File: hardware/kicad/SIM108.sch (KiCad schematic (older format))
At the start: 28 parts, among them J1 Screw_Terminal_01x09, J2 CAN, SW1 PRG, SW2 INSTANCE, SW3 BUS, U1 MCP2551-I-P, U2 TMR_2411, U3 MAX6816, U4 74HC595, U5 Teensy_3.2

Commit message: Stuff
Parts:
- R3: value 4K7 -> 470R
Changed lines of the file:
@@
 P 10150 4300
 F 0 "R3" H 10100 4300 50  0000 R CNN
-F 1 "4K7" V 10150 4300 39  0000 C CNN
+F 1 "470R" V 10150 4300 39  0000 C CNN
 F 2 "Resistor_THT:R_Axial_DIN0207_L6.3mm_D2.5mm_P2.54mm_Vertical" V 10080 4300 50  0001 C CNN
 F 3 "~" H 10150 4300 50  0001 C CNN

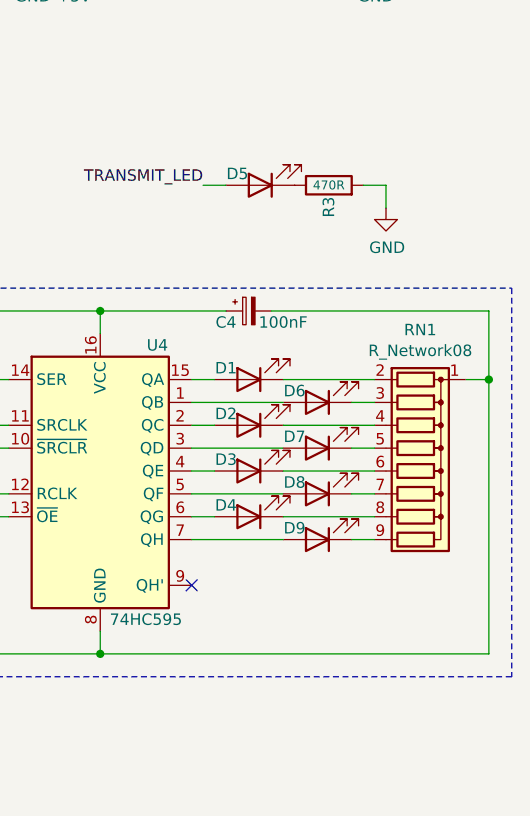
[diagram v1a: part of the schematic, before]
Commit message: Add mount holes
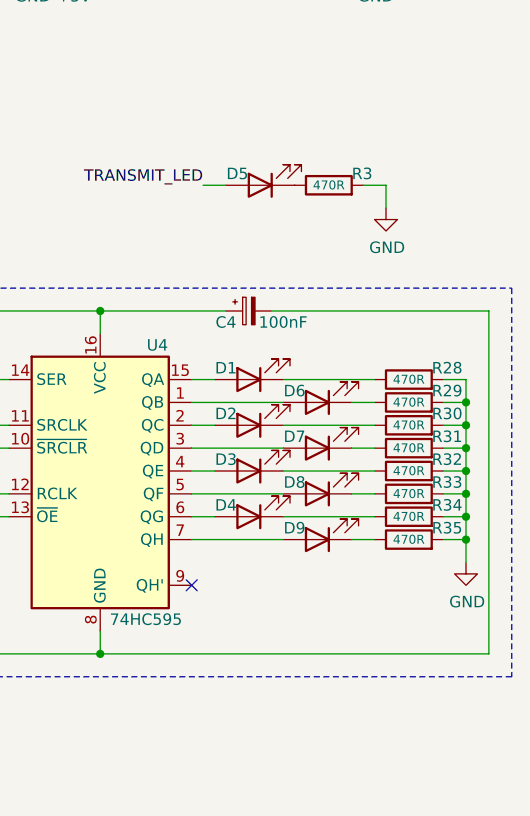
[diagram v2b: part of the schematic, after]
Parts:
- removed RN1: R_Network08, Resistor_THT:R_Array_SIP9, symbol Device:R_Network08
- added R28, R29, R30, R31, R32, R33, R34, R35: 470R, Resistor_THT:R_Axial_DIN0207_L6.3mm_D2.5mm_P2.54mm_Vertical, symbol Device:R
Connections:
- net GND: now also R28.2, R29.2, R30.2, R31.2, R32.2, R33.2, R34.2, R35.2
- net at D1.1 (K): now also R28.1
- net at D6.1 (K): now also R29.1
- net at D2.1 (K): now also R30.1
- net at D7.1 (K): now also R31.1
- net at D4.1 (K): now also R34.1
- net at D9.1 (K): now also R35.1
- net at D3.1 (K): now also R32.1
- net at D8.1 (K): now also R33.1
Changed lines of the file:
@@
 $EndComp
-Wire Wire Line
-	10750 5150 10850 5150
 Wire Wire Line
 	10850 6350 9150 6350
@@
 Wire Wire Line
 	9950 5750 10350 5750
-$Comp
-L Device:R_Network08 RN1
-U 1 1 6337568A
-P 10550 5550
-F 0 "RN1" V 9933 5550 50  0000 C CNN
-F 1 "R_Network08" V 10024 5550 50  0000 C CNN
-F 2 "Resistor_THT:R_Array_SIP9" V 11025 5550 50  0001 C CNN
-F 3 "http://www.vishay.com/docs/31509/csc.pdf" H 10550 5550 50  0001 C CNN
-	1    10550 5550
-	0    1    1    0
-$EndComp
-Wire Wire Line
-	10850 5150 10850 6350
 Wire Wire Line
 	10250 5850 10350 5850
@@
 Wire Wire Line
 	9900 4850 10850 4850
-Wire Wire Line
-	10850 4850 10850 5150
-Connection ~ 10850 5150
 $Comp
 L Switch:SW_Push SW1
@@
 U 1 1 63493E4A
 P 10150 4300
-F 0 "R3" H 10100 4300 50  0000 R CNN
+F 0 "R3" V 10200 4200 50  0000 R CNN
 F 1 "470R" V 10150 4300 39  0000 C CNN
 F 2 "Resistor_THT:R_Axial_DIN0207_L6.3mm_D2.5mm_P2.54mm_Vertical" V 10080 4300 50  0001 C CNN
@@
 	0    -1   1    0
 $EndComp
+$Comp
+L Device:R R28
+U 1 1 634C34EB
+P 10500 5150
+F 0 "R28" V 10550 5050 50  0000 R CNN
+F 1 "470R" V 10500 5150 39  0000 C CNN
+F 2 "Resistor_THT:R_Axial_DIN0207_L6.3mm_D2.5mm_P2.54mm_Vertical" V 10430 5150 50  0001 C CNN
+F 3 "~" H 10500 5150 50  0001 C CNN
+	1    10500 5150
+	0    -1   -1   0
+$EndComp
+$Comp
+L Device:R R29
+U 1 1 634C3A8E
+P 10500 5250
+F 0 "R29" V 10550 5150 50  0000 R CNN
+F 1 "470R" V 10500 5250 39  0000 C CNN
+F 2 "Resistor_THT:R_Axial_DIN0207_L6.3mm_D2.5mm_P2.54mm_Vertical" V 10430 5250 50  0001 C CNN
+F 3 "~" H 10500 5250 50  0001 C CNN
+	1    10500 5250
+	0    -1   -1   0
+$EndComp
+$Comp
+L Device:R R30
+U 1 1 634C3E87
+P 10500 5350
+F 0 "R30" V 10550 5250 50  0000 R CNN
+F 1 "470R" V 10500 5350 39  0000 C CNN
+F 2 "Resistor_THT:R_Axial_DIN0207_L6.3mm_D2.5mm_P2.54mm_Vertical" V 10430 5350 50  0001 C CNN
+F 3 "~" H 10500 5350 50  0001 C CNN
+	1    10500 5350
+	0    -1   -1   0
+$EndComp
+$Comp
+L Device:R R31
+U 1 1 634C42EC
+P 10500 5450
+F 0 "R31" V 10550 5350 50  0000 R CNN
+F 1 "470R" V 10500 5450 39  0000 C CNN
+F 2 "Resistor_THT:R_Axial_DIN0207_L6.3mm_D2.5mm_P2.54mm_Vertical" V 10430 5450 50  0001 C CNN
+F 3 "~" H 10500 5450 50  0001 C CNN
+	1    10500 5450
+	0    -1   -1   0
+$EndComp
+$Comp
+L Device:R R32
+U 1 1 634C469C
+P 10500 5550
+F 0 "R32" V 10550 5450 50  0000 R CNN
+F 1 "470R" V 10500 5550 39  0000 C CNN
+F 2 "Resistor_THT:R_Axial_DIN0207_L6.3mm_D2.5mm_P2.54mm_Vertical" V 10430 5550 50  0001 C CNN
+F 3 "~" H 10500 5550 50  0001 C CNN
+	1    10500 5550
+	0    -1   -1   0
+$EndComp
+$Comp
+L Device:R R33
+U 1 1 634C4AC7
+P 10500 5650
+F 0 "R33" V 10550 5550 50  0000 R CNN
+F 1 "470R" V 10500 5650 39  0000 C CNN
+F 2 "Resistor_THT:R_Axial_DIN0207_L6.3mm_D2.5mm_P2.54mm_Vertical" V 10430 5650 50  0001 C CNN
+F 3 "~" H 10500 5650 50  0001 C CNN
+	1    10500 5650
+	0    -1   -1   0
+$EndComp
+$Comp
+L Device:R R34
+U 1 1 634C4F7E
+P 10500 5750
+F 0 "R34" V 10550 5650 50  0000 R CNN
+F 1 "470R" V 10500 5750 39  0000 C CNN
+F 2 "Resistor_THT:R_Axial_DIN0207_L6.3mm_D2.5mm_P2.54mm_Vertical" V 10430 5750 50  0001 C CNN
+F 3 "~" H 10500 5750 50  0001 C CNN
+	1    10500 5750
+	0    -1   -1   0
+$EndComp
+$Comp
+L Device:R R35
+U 1 1 634C53BF
+P 10500 5850
+F 0 "R35" V 10550 5750 50  0000 R CNN
+F 1 "470R" V 10500 5850 39  0000 C CNN
+F 2 "Resistor_THT:R_Axial_DIN0207_L6.3mm_D2.5mm_P2.54mm_Vertical" V 10430 5850 50  0001 C CNN
+F 3 "~" H 10500 5850 50  0001 C CNN
+	1    10500 5850
+	0    -1   -1   0
+$EndComp
+Wire Wire Line
+	10650 5150 10750 5150
+Wire Wire Line
+	10750 5150 10750 5250
+Wire Wire Line
+	10750 5850 10650 5850
+Wire Wire Line
+	10850 4850 10850 6350
+Wire Wire Line
+	10750 5850 10750 5950
+Connection ~ 10750 5850
+$Comp
+L power:GND #PWR029
+U 1 1 634F8D12
+P 10750 5950
+F 0 "#PWR029" H 10750 5700 50  0001 C CNN
+F 1 "GND" H 10755 5777 50  0000 C CNN
+F 2 "" H 10750 5950 50  0001 C CNN
+F 3 "" H 10750 5950 50  0001 C CNN
+	1    10750 5950
+	1    0    0    -1
+$EndComp
+Wire Wire Line
+	10650 5250 10750 5250
+Connection ~ 10750 5250
+Wire Wire Line
+	10750 5250 10750 5350
+Wire Wire Line
+	10650 5350 10750 5350
+Connection ~ 10750 5350
+Wire Wire Line
+	10750 5350 10750 5450
+Wire Wire Line
+	10650 5450 10750 5450
+Connection ~ 10750 5450
+Wire Wire Line
+	10750 5450 10750 5550
+Wire Wire Line
+	10650 5550 10750 5550
+Connection ~ 10750 5550
+Wire Wire Line
+	10750 5550 10750 5650
+Wire Wire Line
+	10650 5650 10750 5650
+Connection ~ 10750 5650
+Wire Wire Line
+	10750 5650 10750 5750
+Wire Wire Line
+	10650 5750 10750 5750
+Connection ~ 10750 5750
+Wire Wire Line
+	10750 5750 10750 5850
 $EndSCHEMATC

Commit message: Change to Camden Boss connector
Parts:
- J1: footprint PDJR-connectors:RS-PLUG-TERMINAL-HORIZ-9-PIN -> PDJR-connectors:CAMDEN_BOSS_CSTBV2-9_TERMINAL
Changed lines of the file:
@@
 F 0 "J1" H 800 2700 50  0000 C CNN
 F 1 "Screw_Terminal_01x09" H 800 2700 50  0001 C CNN
-F 2 "PDJR-connectors:RS-PLUG-TERMINAL-HORIZ-9-PIN" H 800 2200 50  0001 C CNN
+F 2 "PDJR-connectors:CAMDEN_BOSS_CSTBV2-9_TERMINAL" H 800 2200 50  0001 C CNN
 F 3 "~" H 800 2200 50  0001 C CNN
 	1    800  2200

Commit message: Refactor
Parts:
- U2: footprint PDJR-connectors:TMR_2411 -> PDJR_DC-DC_Converters:TMR_2411
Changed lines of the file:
@@
 F 0 "U2" H 2900 5500 50  0000 C CNN
 F 1 "TMR_2411" H 2900 4800 50  0000 C CNN
-F 2 "PDJR-connectors:TMR_2411" H 2900 4800 50  0001 C CNN
+F 2 "PDJR_DC-DC_Converters:TMR_2411" H 2900 4800 50  0001 C CNN
 F 3 "" H 2900 4650 50  0001 C CNN
 	1    2900 5150

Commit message: Refactor
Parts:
- J1: footprint PDJR-connectors:CAMDEN_BOSS_CSTBV2-9_TERMINAL -> PDJR_Connectors:CAMDEN_BOSS_CSTBV2-9_TERMINAL
- SW1: footprint PDJR-connectors:PCB_PUSH_BUTTON -> PDJR_Switches:PCB_PUSH_BUTTON_10mm
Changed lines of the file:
@@
 F 0 "J1" H 800 2700 50  0000 C CNN
 F 1 "Screw_Terminal_01x09" H 800 2700 50  0001 C CNN
-F 2 "PDJR-connectors:CAMDEN_BOSS_CSTBV2-9_TERMINAL" H 800 2200 50  0001 C CNN
+F 2 "PDJR_Connectors:CAMDEN_BOSS_CSTBV2-9_TERMINAL" H 800 2200 50  0001 C CNN
 F 3 "~" H 800 2200 50  0001 C CNN
 	1    800  2200
@@
 F 0 "SW1" H 5500 7300 50  0000 C CNN
 F 1 "PRG" H 5500 7000 50  0000 C CNN
-F 2 "PDJR-connectors:PCB_PUSH_BUTTON" H 5500 7300 50  0001 C CNN
+F 2 "PDJR_Switches:PCB_PUSH_BUTTON_10mm" H 5500 7300 50  0001 C CNN
 F 3 "~" H 5500 7300 50  0001 C CNN
 	1    5500 7100

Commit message: Add jumper alternative to SW2
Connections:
- net CAN_L: now also SW3.4; no longer SW3.3
- net CAN_SCR: now also SW3.3; no longer SW3.4
- net GND: now also SW3.2; no longer SW3.1
- net TERM_A: now also SW3.1; no longer SW3.2
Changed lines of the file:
@@
 L Switch:SW_DIP_x02 SW3
 U 1 1 62A67242
-P 5800 6150
-F 0 "SW3" H 5800 6000 50  0000 C CNN
-F 1 "BUS" H 5800 6400 50  0000 C CNN
-F 2 "Package_DIP:DIP-4_W7.62mm_LongPads" H 5800 6150 50  0001 C CNN
-F 3 "~" H 5800 6150 50  0001 C CNN
-	1    5800 6150
-	1    0    0    1
+P 5800 6250
+F 0 "SW3" H 5800 6100 50  0000 C CNN
+F 1 "BUS" H 5800 6500 50  0000 C CNN
+F 2 "Package_DIP:DIP-4_W7.62mm_LongPads" H 5800 6250 50  0001 C CNN
+F 3 "~" H 5800 6250 50  0001 C CNN
+	1    5800 6250
+	1    0    0    -1
 $EndComp
 Wire Wire Line

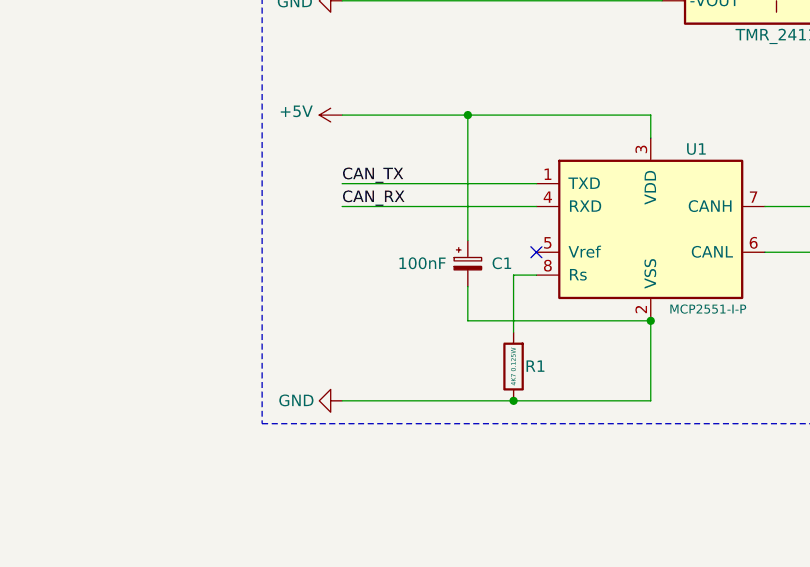
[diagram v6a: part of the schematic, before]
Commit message: Revise for 3.3V
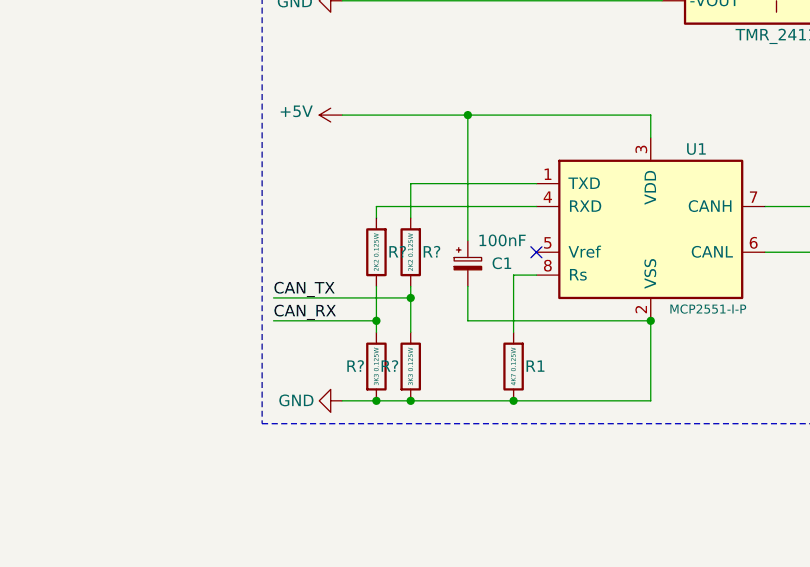
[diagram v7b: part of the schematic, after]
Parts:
- added R? (x2): 2K2 0.125W, Resistor_THT:R_Axial_DIN0207_L6.3mm_D2.5mm_P2.54mm_Vertical, symbol Device:R
- added R? (x2): 3K3 0.125W, Resistor_THT:R_Axial_DIN0207_L6.3mm_D2.5mm_P2.54mm_Vertical, symbol Device:R
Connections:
- net CAN_RX: now also R?.1, R?.1; no longer U1.4 (RXD)
- net CAN_TX: now also R?.1, R?.1; no longer U1.1 (TXD)
- net GND: now also R?.2, R?.2
- new net: R?.2, U1.1 (TXD)
- new net: R?.2, U1.4 (RXD)
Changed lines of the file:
@@
 NET_C
-Wire Wire Line
-	1000 6250 1850 6250
 Wire Wire Line
 	2350 6750 2350 7100
@@
 	1000 5850 1550 5850
 Wire Wire Line
-	1000 7100 1750 7100
-Text Label 1000 6250 0    50   ~ 0
+	1000 7100 1150 7100
+Text Label 700  6750 0    50   ~ 0
 CAN_RX
-Text Label 1000 6150 0    50   ~ 0
+Text Label 700  6650 0    50   ~ 0
 CAN_TX
-Wire Wire Line
-	1000 6150 1850 6150
 Wire Wire Line
 	3900 7100 3900 6900
@@
 P 1550 6500
 F 0 "C1" H 1700 6500 50  0000 C CNN
-F 1 "100nF" H 1350 6500 50  0000 C CNN
+F 1 "100nF" H 1700 6600 50  0000 C CNN
 F 2 "Capacitor_THT:CP_Radial_D5.0mm_P2.00mm" H 1550 6500 50  0001 C CNN
 F 3 "~" H 1550 6500 50  0001 C CNN
@@
 Wire Wire Line
 	10750 5750 10750 5850
+$Comp
+L Device:R R?
+U 1 1 638A66B7
+P 1300 6450
+F 0 "R?" H 1250 6450 50  0000 R CNN
+F 1 "2K2 0.125W" V 1300 6450 20  0000 C CNN
+F 2 "Resistor_THT:R_Axial_DIN0207_L6.3mm_D2.5mm_P2.54mm_Vertical" V 1230 6450 50  0001 C CNN
+F 3 "~" H 1300 6450 50  0001 C CNN
+	1    1300 6450
+	-1   0    0    1
+$EndComp
+$Comp
+L Device:R R?
+U 1 1 638A701E
+P 1300 6950
+F 0 "R?" H 1250 6950 50  0000 R CNN
+F 1 "3K3 0.125W" V 1300 6950 20  0000 C CNN
+F 2 "Resistor_THT:R_Axial_DIN0207_L6.3mm_D2.5mm_P2.54mm_Vertical" V 1230 6950 50  0001 C CNN
+F 3 "~" H 1300 6950 50  0001 C CNN
+	1    1300 6950
+	1    0    0    -1
+$EndComp
+Connection ~ 1300 7100
+Wire Wire Line
+	1300 7100 1750 7100
+Wire Wire Line
+	1300 6300 1300 6150
+Wire Wire Line
+	1300 6150 1850 6150
+Wire Wire Line
+	1300 6600 1300 6650
+Wire Wire Line
+	700  6650 1300 6650
+Connection ~ 1300 6650
+Wire Wire Line
+	1300 6650 1300 6800
+$Comp
+L Device:R R?
+U 1 1 638DB685
+P 1150 6450
+F 0 "R?" H 1100 6450 50  0000 R CNN
+F 1 "2K2 0.125W" V 1150 6450 20  0000 C CNN
+F 2 "Resistor_THT:R_Axial_DIN0207_L6.3mm_D2.5mm_P2.54mm_Vertical" V 1080 6450 50  0001 C CNN
+F 3 "~" H 1150 6450 50  0001 C CNN
+	1    1150 6450
+	-1   0    0    1
+$EndComp
+$Comp
+L Device:R R?
+U 1 1 638DBDD6
+P 1150 6950
+F 0 "R?" H 1100 6950 50  0000 R CNN
+F 1 "3K3 0.125W" V 1150 6950 20  0000 C CNN
+F 2 "Resistor_THT:R_Axial_DIN0207_L6.3mm_D2.5mm_P2.54mm_Vertical" V 1080 6950 50  0001 C CNN
+F 3 "~" H 1150 6950 50  0001 C CNN
+	1    1150 6950
+	1    0    0    -1
+$EndComp
+Connection ~ 1150 7100
+Wire Wire Line
+	1150 7100 1300 7100
+Wire Wire Line
+	1150 6600 1150 6750
+Wire Wire Line
+	1150 6750 700  6750
+Connection ~ 1150 6750
+Wire Wire Line
+	1150 6750 1150 6800
+Wire Wire Line
+	1150 6300 1150 6250
+Wire Wire Line
+	1150 6250 1850 6250
 $EndSCHEMATC
